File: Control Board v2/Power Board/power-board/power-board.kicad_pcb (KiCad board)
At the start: 6 copper layers, 92 x 118.5 mm, 26 parts, among them J1 1366005, J2 1366005, J6 Conn_01x04, J7 Conn_01x02, SW1 SW_SPST, U2 MOC3083S-TA1

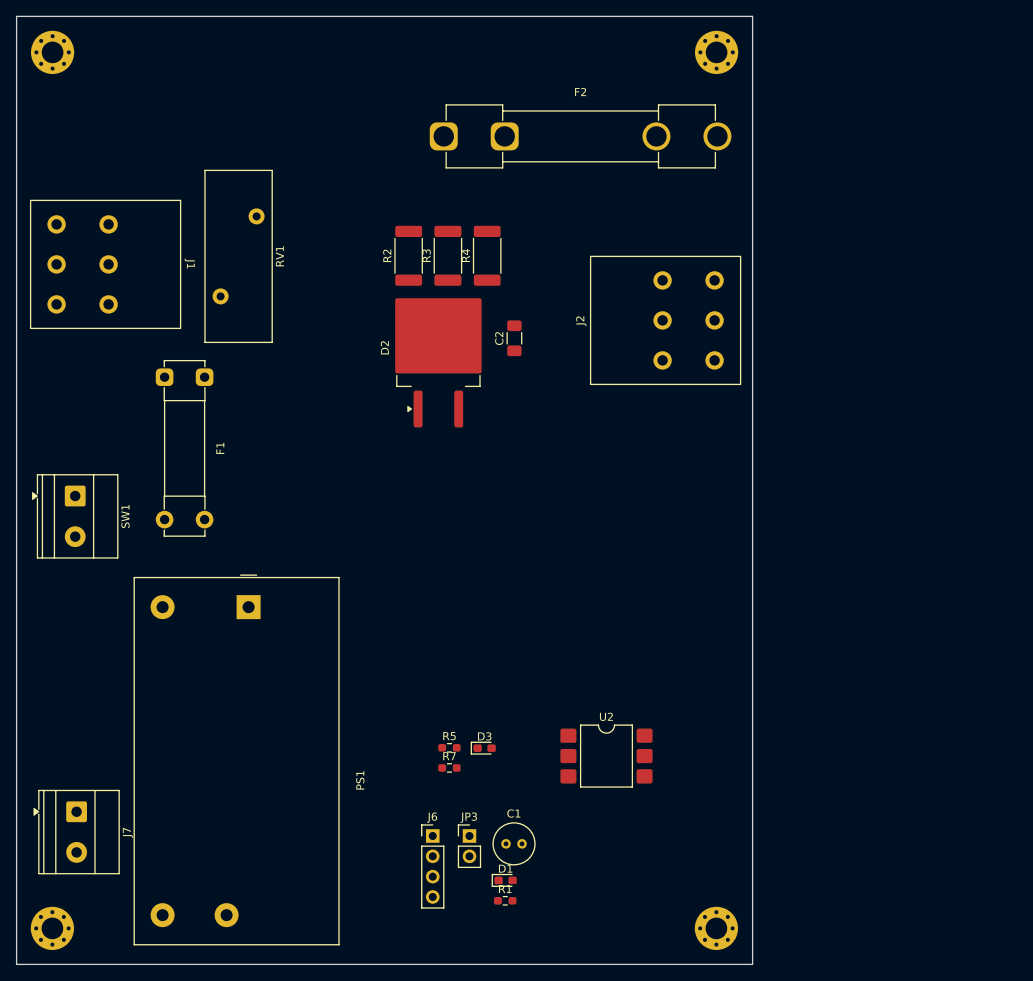
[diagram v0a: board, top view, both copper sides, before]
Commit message: add isolation to pcb design
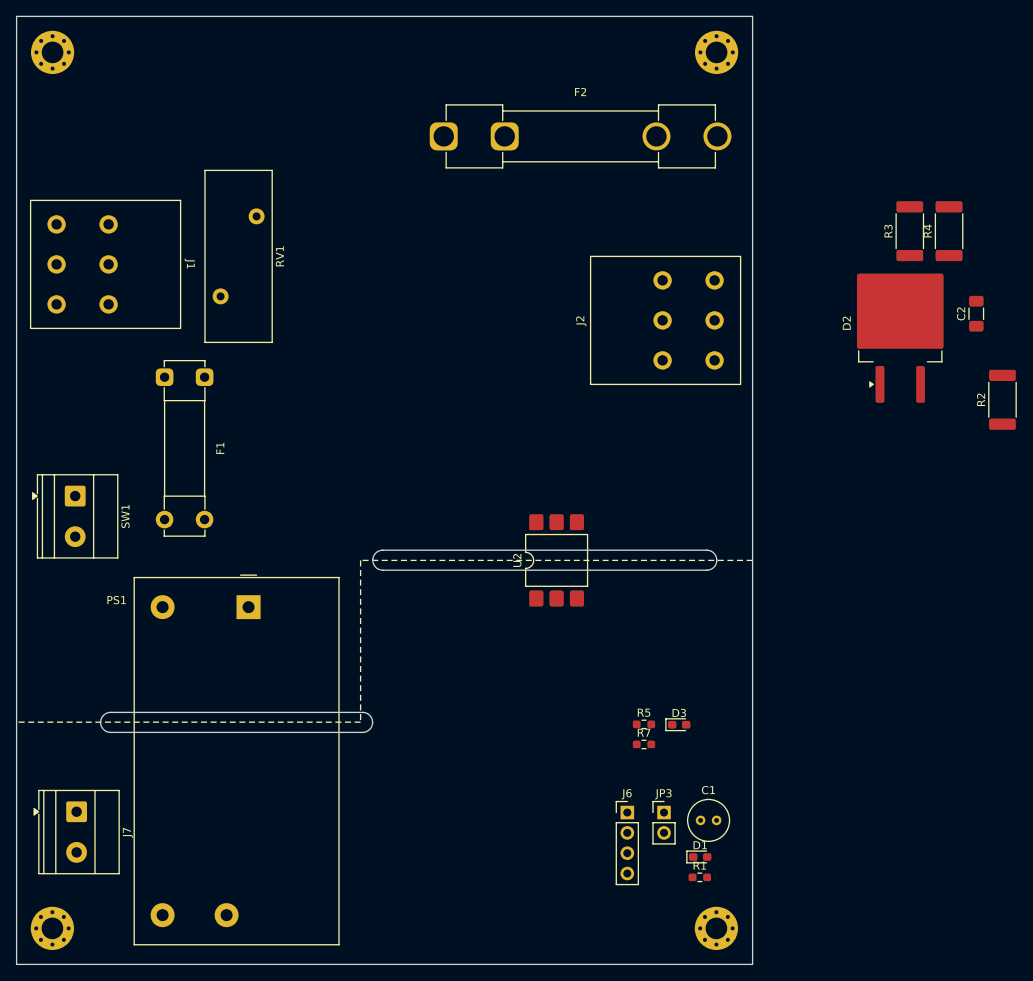
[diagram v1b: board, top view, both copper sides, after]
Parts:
- moved R2 76.4 mm to (236.7, 70.9)
- moved C2 57.8 mm to (233.5, 60.2)
- moved D2 57.8 mm to (224.0, 61.4)
- moved R3 57.8 mm to (225.2, 49.9)
- moved R4 57.8 mm to (230.1, 49.9)
- moved U2 25.2 mm to (181.0, 91.0), turned to 90 degrees
- moved R5 24.5 mm to (191.9, 111.5)
- moved R7 24.5 mm to (191.9, 114.0)
- moved C1 24.5 mm to (199.0, 123.5)
- moved D1 24.5 mm to (198.9, 128.1)
- moved D3 24.5 mm to (196.3, 111.5)
- moved J6 24.5 mm to (189.8, 122.5)
- moved JP3 24.5 mm to (194.4, 122.5)
- moved R1 24.5 mm to (198.9, 130.6)
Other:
- outline, holes or cut-outs redrawn

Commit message: pcb design
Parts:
- F1: footprint Fuse:Fuseholder_Clip-5x20mm_Bel_FC-203-22_Lateral_P17.80x5.00mm_D1.17mm_Horizontal -> Fuse:Fuseholder_Clip-5x20mm_Littelfuse_100_Inline_P20.50x4.60mm_D1.30mm_Horizontal
- RV1: footprint Varistor:RV_Disc_D21.5mm_W8.4mm_P10mm -> TMOV20RP150E:TMOV20RP150E
- moved C2 58.4 mm to (175.3, 65.4)
- moved D2 58.4 mm to (165.8, 66.6)
- moved R2 58.4 mm to (178.6, 76.2)
- moved R3 58.4 mm to (167.0, 55.1)
- moved R4 58.4 mm to (171.9, 55.1)
- moved RV1 3.63 mm to (142.6, 57.8)

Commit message: PCB layout is generally complete
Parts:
- removed J6: Conn_01x04, Connector_PinHeader_2.54mm:PinHeader_1x04_P2.54mm_Vertical
- added G***: LOGO, LOGO, F.Cu at (149.0, 73.5)
- added G***: LOGO, LOGO, F.Cu at (125.0, 112.0)
- added G***: LOGO, LOGO, B.Cu at (147.5, 106.5)
- added G***: LOGO, LOGO, B.Cu at (178.5, 73.5)
- added J3: Conn_01x03, Connector_PinHeader_2.54mm:PinHeader_1x03_P2.54mm_Vertical, F.Cu at (203.0, 91.5)
- added REF**: MTP Logo 10mm Low Detail, Watermarks:MTP Logo 10mm Low Detail, F.Cu at (134.0, 87.0)
- C2: footprint Capacitor_SMD:C_1206_3216Metric_Pad1.33x1.80mm_HandSolder -> Capacitor_SMD:C_1812_4532Metric_Pad1.57x3.40mm_HandSolder
- H1, H2, H3, H4: footprint MountingHole:MountingHole_2.7mm_M2.5_Pad_Via -> MountingHole:MountingHole_2.5mm
- moved J7 65.8 mm to (186.4, 115.5), turned to 0 degrees
- moved C2 42.3 mm to (143.5, 37.5), turned to 180 degrees
- moved R7 28.8 mm to (198.5, 86.0)
- moved R1 28.1 mm to (199.0, 102.5)
- moved R4 26.5 mm to (152.0, 37.5), turned to 0 degrees
- moved R2 26.1 mm to (156.0, 63.0), turned to 0 degrees
- moved D1 25.9 mm to (195.1, 102.5), turned to 180 degrees
- moved JP3 25.1 mm to (180.0, 102.0), turned to 90 degrees
- moved C1 24.4 mm to (188.5, 101.5), turned to 90 degrees
- moved D3 22.6 mm to (195.5, 89.0), turned to -90 degrees
- moved R5 21.5 mm to (192.1, 90.0), turned to 180 degrees
- moved H3 20.0 mm to (118.0, 117.0)
- moved H4 20.0 mm to (201.0, 117.0)
- moved U2 16.5 mm to (165.0, 87.0), turned to 180 degrees
- moved D2 15.6 mm to (166.2, 51.0), turned to 0 degrees
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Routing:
- net GNDPWR: track 0.00 -> 94.7 mm, vias 0 -> 1
- net LN: track 0.00 -> 60.5 mm
- net /Project Architecture/Heater Control/LN_OPTO: track 0.00 -> 41.8 mm, vias 0 -> 2
- net VDD: track 0.00 -> 38.1 mm
- net /Project Architecture/Power Supply/L1_F1_SW: track 0.00 -> 33.7 mm
- net /Project Architecture/Heater Control/L1_F2_OPTO: track 0.00 -> 31.6 mm, vias 0 -> 2
- net /Project Architecture/Heater Control/D_R5_OPTO: track 0.00 -> 21.6 mm
- net /Project Architecture/Power Supply/L1_F1: track 0.00 -> 15.4 mm
- net D_Heater: track 0.00 -> 12.7 mm
- net /Project Architecture/Power Supply/VDD_AC_DC: track 0.00 -> 10.2 mm
- net GND: track 0.00 -> 6.41 mm, vias 0 -> 3
- net /Project Architecture/Heater Control/D3_K: track 0.00 -> 2.99 mm
- net /Project Architecture/Power Supply/D1_K: track 0.00 -> 2.09 mm
- net /Project Architecture/Heater Control/L1_F2: vias 0 -> 428
- added copper zone on F.Cu, net /Project Architecture/Heater Control/L1_F2
- added copper zone on F.Cu, net /Project Architecture/Heater Control/L1_F2_RC
- added copper zone on F.Cu, net /Project Architecture/Heater Control/L1_HEATER
- added copper zone on B.Cu, net GND
- added copper zone on F.Cu, net L1
- added copper zone on F.Cu, net LN
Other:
- board size 92 x 118.5 mm -> 92 x 91.5 mm
- copper layers 6 -> 2
- board text added: "+"
- board text added: "-"
- board text added: "1A"
- board text added: "20A"
- board text added: "5V"
- board text added: "5v"
- board text added: "AC Power Switch for 5V PSU"
- board text added: "Aux. 5v Input"
- board text added: "CAUTION 120VAC"
- board text added: "COLD"
- board text added: "Caution! Mains Voltage"
- board text added: "Des. by Michael Pate v2.0 09/2025"
- board text added: "GND"
- board text added: "HOT"
- board text added: "High Voltage! Disconnect AC before programming."
- board text added: "L"
- board text added: "N"
- board text added: "PROTOTYPE"
- board text added: "Remove JP3 for Aux. 5v input!"
- board text added: "SIG"
- board text added: "TRIAC Heater Control"

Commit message: generate production files
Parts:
- J3: footprint Connector_PinHeader_2.54mm:PinHeader_1x03_P2.54mm_Vertical -> Connector_JST:JST_PH_B3B-PH-K_1x03_P2.00mm_Vertical
- moved R7 3.20 mm to (196.0, 88.0)
- moved D3 3.05 mm to (192.5, 89.2)
- moved R5 3.05 mm to (189.0, 90.2)
- moved J3 0.70 mm to (202.6, 92.0), turned to -90 degrees
- moved C1 0.50 mm to (188.5, 102.0)
- moved D1 0.50 mm to (195.1, 102.0)
- moved R1 0.50 mm to (199.0, 102.0)
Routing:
- net /Project Architecture/Heater Control/D_R5_OPTO: track 21.6 -> 18.6 mm
- net D_Heater: track 12.7 -> 14.7 mm
- net /Project Architecture/Heater Control/LN_OPTO: track 41.8 -> 43.3 mm
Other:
- board text removed: "5v"
